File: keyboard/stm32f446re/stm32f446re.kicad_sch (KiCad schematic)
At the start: 22 parts

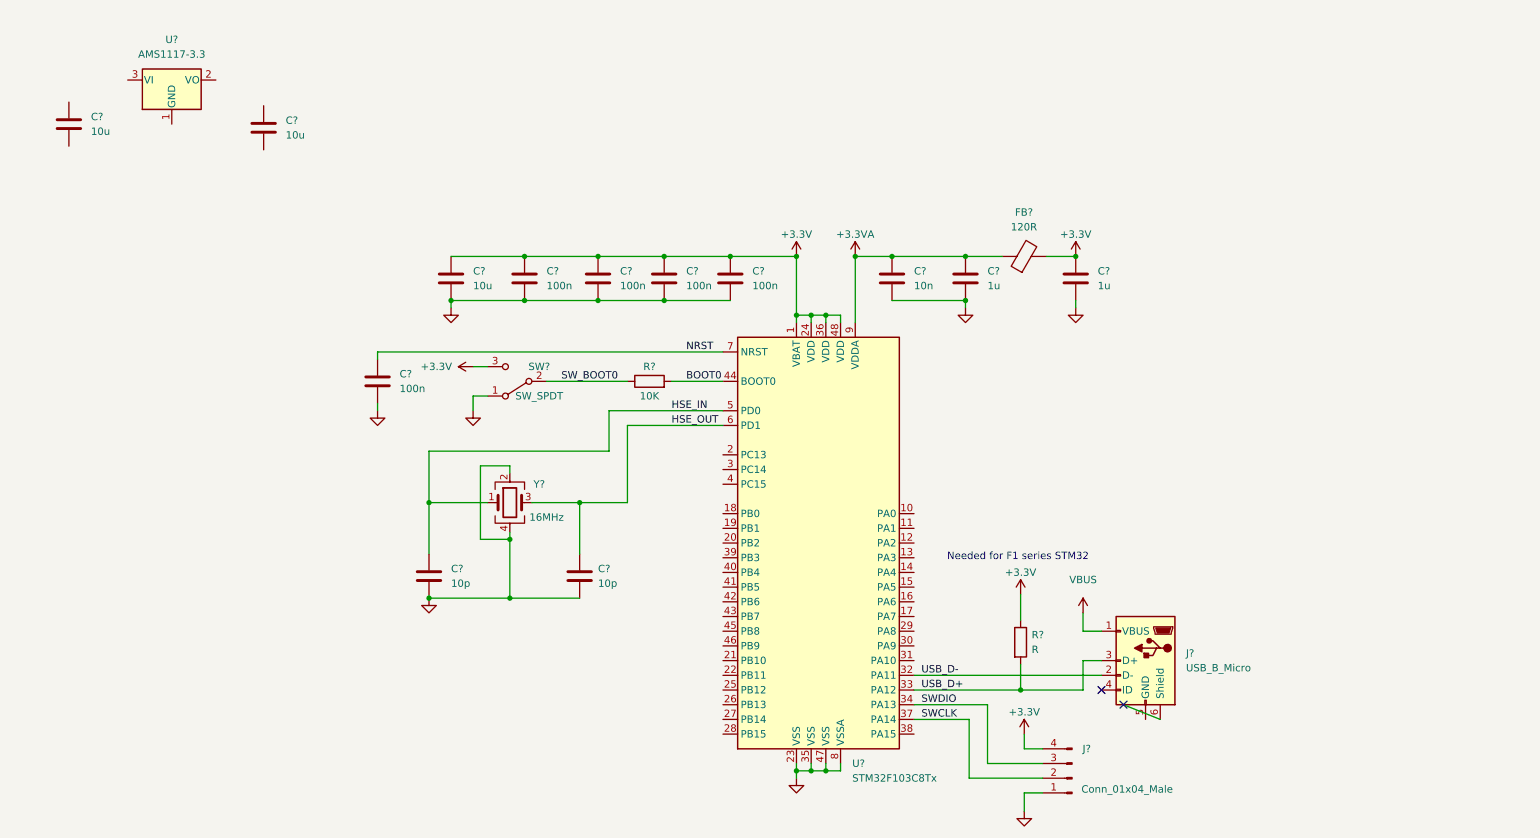
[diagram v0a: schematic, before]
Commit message: Working on STMF103 schematic
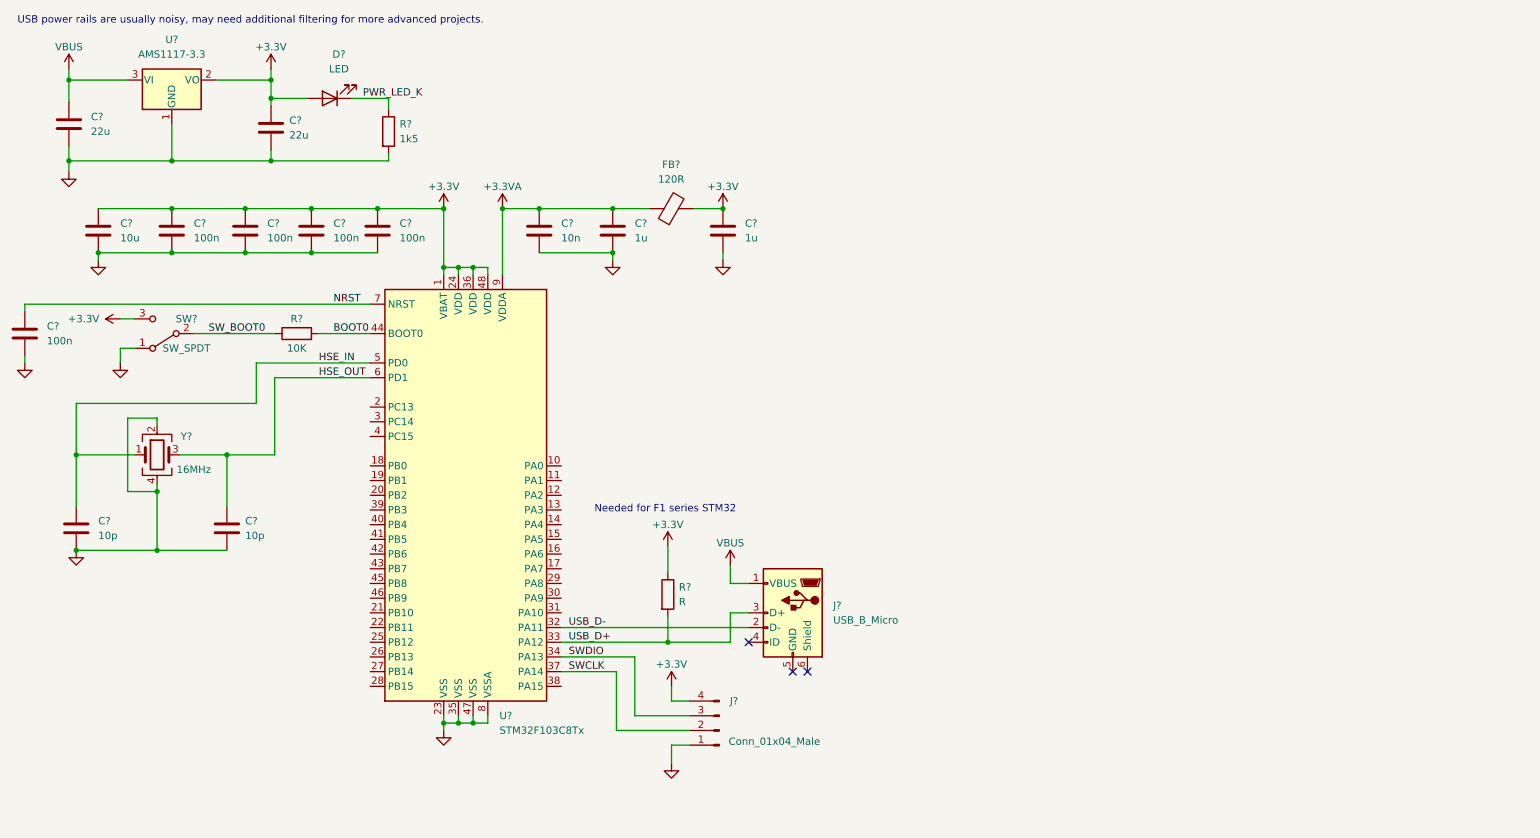
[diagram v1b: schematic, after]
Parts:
- added D?: LED, symbol Device:LED
- added R?: 1k5, symbol Device:R
- C? (x2): value 10u -> 22u
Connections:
- net +3.3V: now also C?.1, U?.2 (VO), D?.2 (A)
- net GND: now also C?.2, C?.2, U?.1 (GND), R?.2
- net VBUS: now also C?.1, U?.3 (VI)
- new net PWR_LED_K: D?.1 (K), R?.1
- no-connect marks 2 -> 3
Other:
- note added: "USB power rails are usually noisy, may need additional filtering for more advanced projects."
- moved on the sheet: C?, FB?, J?, R?, SW?, U?, Y?

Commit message: Preparing to auto-annotate schematic
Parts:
- added D? (x16): 1N4148, Diode_THT:D_DO-35_SOD27_P7.62mm_Horizontal, symbol Diode:1N4148
- added SW? (x16): SW_Push, symbol Switch:SW_Push
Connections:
- net COL0: now reaches U?.10 (PA0)
- net COL0: now also SW?.2, SW?.2, SW?.2, SW?.2
- net COL1: now reaches U?.11 (PA1)
- net COL1: now also SW?.2, SW?.2, SW?.2, SW?.2
- net COL2: now reaches U?.12 (PA2)
- net COL2: now also SW?.2, SW?.2, SW?.2, SW?.2
- net COL3: now reaches U?.13 (PA3)
- net COL3: now also SW?.2, SW?.2, SW?.2, SW?.2
- net ROW0: now reaches U?.14 (PA4)
- net ROW0: now also D?.1 (K), D?.1 (K), D?.1 (K), D?.1 (K)
- net ROW1: now reaches U?.15 (PA5)
- net ROW1: now also D?.1 (K), D?.1 (K), D?.1 (K), D?.1 (K)
- net ROW2: now reaches U?.16 (PA6)
- net ROW2: now also D?.1 (K), D?.1 (K), D?.1 (K), D?.1 (K)
- net ROW3: now reaches U?.17 (PA7)
- net ROW3: now also D?.1 (K), D?.1 (K), D?.1 (K), D?.1 (K)
- new net: D?.2 (A), SW?.1 (x16)
- no-connect marks 3 -> 25
